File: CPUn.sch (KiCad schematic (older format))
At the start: 10 parts, among them J4 JTAG

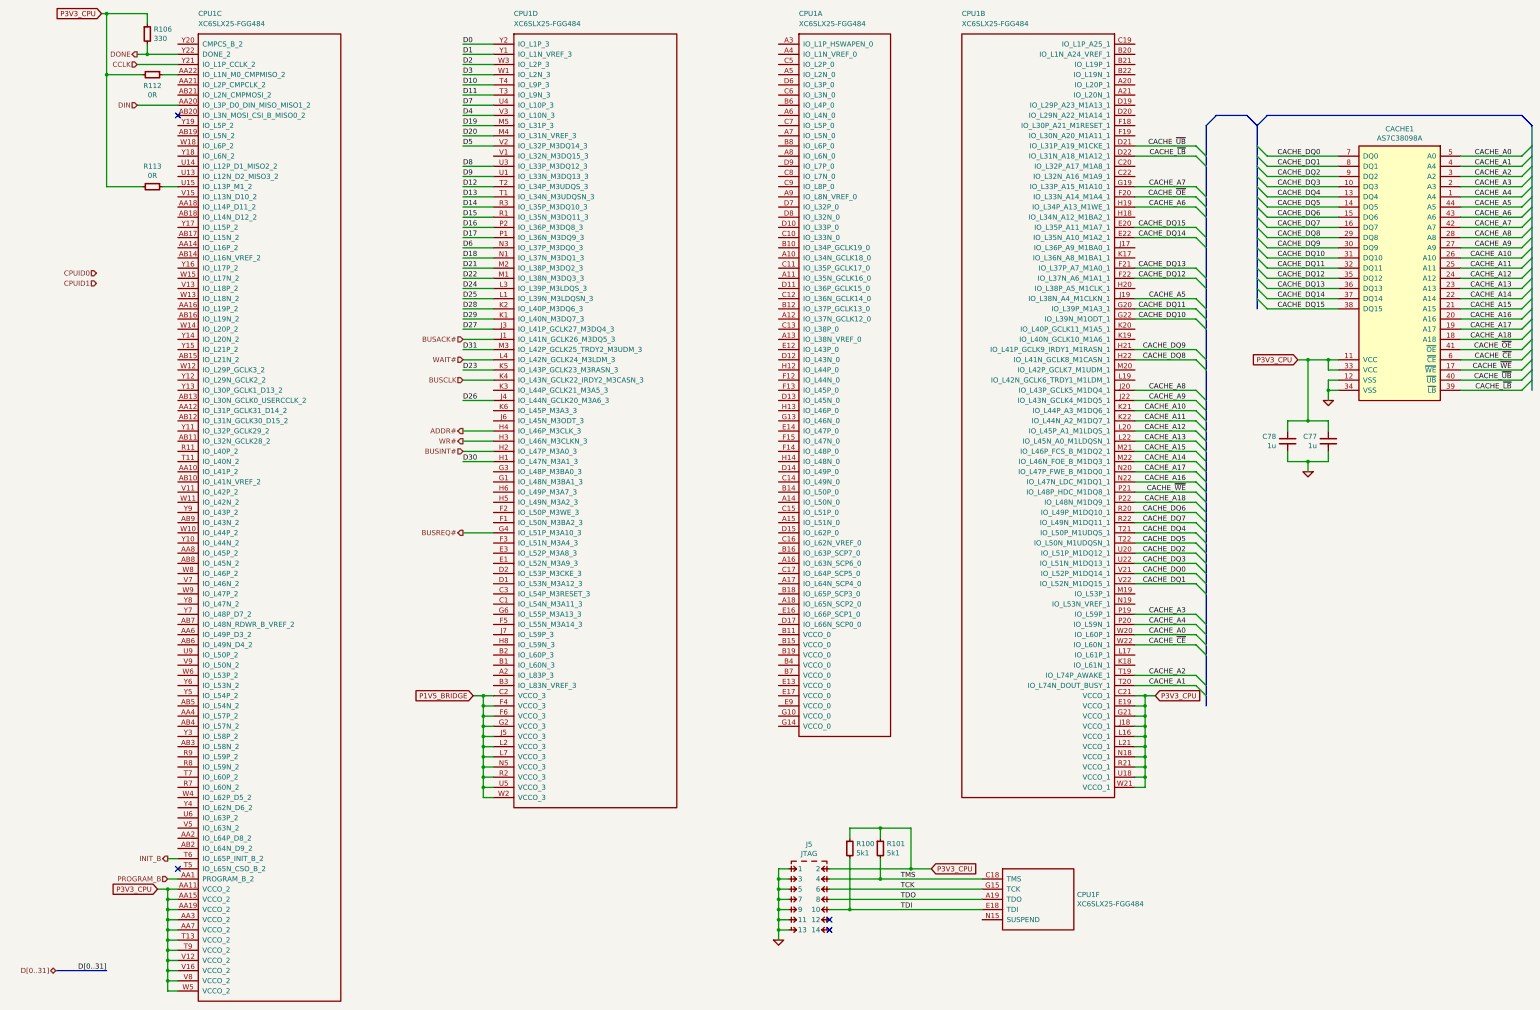
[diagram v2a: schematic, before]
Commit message: Route FPGA suspend signals
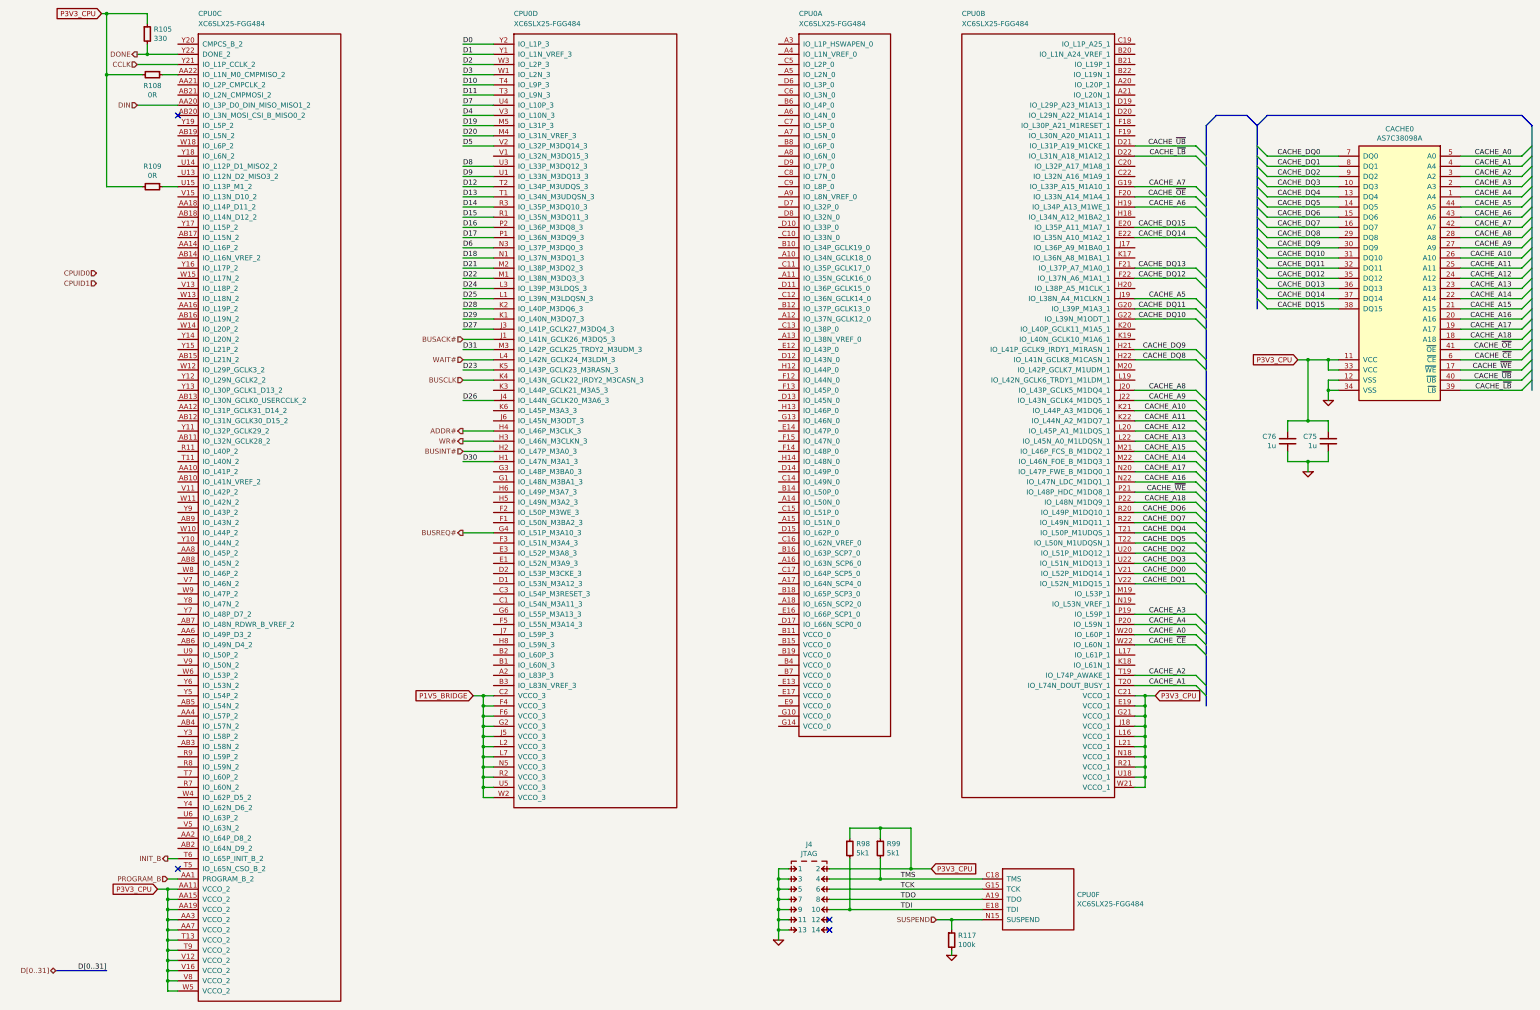
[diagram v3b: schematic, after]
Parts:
- added R117: 100k, IPC7351-Nominal:RESC1005X40, symbol R-0402
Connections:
- net GND: now also R117.2
- net SUSPEND: now reaches CPU0.N15 (SUSPEND)
- net SUSPEND: now also R117.1
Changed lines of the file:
@@
 AR Path="/5765A5BA/577B458D" Ref="CPU0"  Part="3"
 AR Path="/5765B2E6/577B458D" Ref="CPU1"  Part="3"
-F 0 "CPU1" H 2500 1300 50  0000 L CNN
+F 0 "CPU0" H 2500 1300 50  0000 L CNN
 F 1 "XC6SLX25-FGG484" H 2500 1200 50  0000 L CNN
 F 2 "manuf:XILINX-FGG484" H 2400 1150 50  0001 C CNN
@@
 AR Path="/5765A5BA/5783D342" Ref="CACHE0"  Part="1"
 AR Path="/5765B2E6/5783D342" Ref="CACHE1"  Part="1"
-F 0 "CACHE1" H 14300 2367 50  0000 C CNN
+F 0 "CACHE0" H 14300 2367 50  0000 C CNN
 F 1 "AS7C38098A" H 14300 2276 50  0000 C CNN
 F 2 "IPC7351-Nominal:SOP80P1176X120-44" H 14300 -400 50  0001 C CNN
@@
 P3V3_CPU
 $Comp
-L GND #PWR121
+L GND #PWR122
 U 1 1 5793B4AE
 P 13600 4500
-AR Path="/5765A5BA/5793B4AE" Ref="#PWR121"  Part="1"
-AR Path="/5765B2E6/5793B4AE" Ref="#PWR181"  Part="1"
-F 0 "#PWR181" H 13600 4500 30  0001 C CNN
+AR Path="/5765A5BA/5793B4AE" Ref="#PWR122"  Part="1"
+AR Path="/5765B2E6/5793B4AE" Ref="#PWR184"  Part="1"
+F 0 "#PWR122" H 13600 4500 30  0001 C CNN
 F 1 "GND" H 13600 4430 30  0001 C CNN
 F 2 "" H 13600 4500 60  0000 C CNN
@@
 AR Path="/5765A5BA/5793BAAD" Ref="C75"  Part="1"
 AR Path="/5765B2E6/5793BAAD" Ref="C77"  Part="1"
-F 0 "C77" H 13712 4946 50  0000 L CNN
+F 0 "C75" H 13712 4946 50  0000 L CNN
 F 1 "1u" H 13712 4855 50  0000 L CNN
 F 2 "IPC7351-Nominal:CAPC1005X55" H 13600 4900 50  0001 C CNN
@@
 AR Path="/5765A5BA/5793BB4A" Ref="C76"  Part="1"
 AR Path="/5765B2E6/5793BB4A" Ref="C78"  Part="1"
-F 0 "C78" H 13313 4946 50  0000 L CNN
+F 0 "C76" H 13313 4946 50  0000 L CNN
 F 1 "1u" H 13313 4855 50  0000 L CNN
 F 2 "IPC7351-Nominal:CAPC1005X55" H 13200 4900 50  0001 C CNN
@@
 $EndComp
 $Comp
-L GND #PWR120
+L GND #PWR121
 U 1 1 5793BC86
 P 13400 5200
-AR Path="/5765A5BA/5793BC86" Ref="#PWR120"  Part="1"
-AR Path="/5765B2E6/5793BC86" Ref="#PWR180"  Part="1"
-F 0 "#PWR180" H 13400 5200 30  0001 C CNN
+AR Path="/5765A5BA/5793BC86" Ref="#PWR121"  Part="1"
+AR Path="/5765B2E6/5793BC86" Ref="#PWR183"  Part="1"
+F 0 "#PWR121" H 13400 5200 30  0001 C CNN
 F 1 "GND" H 13400 5130 30  0001 C CNN
 F 2 "" H 13400 5200 60  0000 C CNN
@@
 AR Path="/5765A5BA/57942A58" Ref="CPU0"  Part="4"
 AR Path="/5765B2E6/57942A58" Ref="CPU1"  Part="4"
-F 0 "CPU1" H 5600 1300 50  0000 L CNN
+F 0 "CPU0" H 5600 1300 50  0000 L CNN
 F 1 "XC6SLX25-FGG484" H 5600 1200 50  0000 L CNN
 F 2 "manuf:XILINX-FGG484" H 5500 1150 50  0001 C CNN
@@
 AR Path="/5765A5BA/5795C53B" Ref="CPU0"  Part="1"
 AR Path="/5765B2E6/5795C53B" Ref="CPU1"  Part="1"
-F 0 "CPU1" H 8400 1300 50  0000 L CNN
+F 0 "CPU0" H 8400 1300 50  0000 L CNN
 F 1 "XC6SLX25-FGG484" H 8400 1200 50  0000 L CNN
 F 2 "manuf:XILINX-FGG484" H 8300 1150 50  0001 C CNN
@@
 AR Path="/5765A5BA/5795C751" Ref="CPU0"  Part="2"
 AR Path="/5765B2E6/5795C751" Ref="CPU1"  Part="2"
-F 0 "CPU1" H 13400 1300 50  0000 R CNN
+F 0 "CPU0" H 13400 1300 50  0000 R CNN
 F 1 "XC6SLX25-FGG484" H 13400 1200 50  0000 R CNN
 F 2 "manuf:XILINX-FGG484" H 11800 1150 50  0001 C CNN
@@
 AR Path="/5765A5BA/57A58F79" Ref="R105"  Part="1"
 AR Path="/5765B2E6/57A58F79" Ref="R106"  Part="1"
-F 0 "R106" H 2063 946 50  0000 L CNN
+F 0 "R105" H 2063 946 50  0000 L CNN
 F 1 "330" H 2063 855 50  0000 L CNN
 F 2 "IPC7351-Nominal:RESC1005X40" H 2000 900 50  0001 C CNN
@@
 AR Path="/5765A5BA/57A5D20B" Ref="R108"  Part="1"
 AR Path="/5765B2E6/57A5D20B" Ref="R112"  Part="1"
-F 0 "R112" V 2158 1300 50  0000 C CNN
+F 0 "R108" V 2158 1300 50  0000 C CNN
 F 1 "0R" V 2249 1300 50  0000 C CNN
 F 2 "IPC7351-Nominal:RESC1005X40" H 2050 1300 50  0001 C CNN
@@
 AR Path="/5765A5BA/57A5D251" Ref="R109"  Part="1"
 AR Path="/5765B2E6/57A5D251" Ref="R113"  Part="1"
-F 0 "R113" V 1850 2400 50  0000 C CNN
+F 0 "R109" V 1850 2400 50  0000 C CNN
 F 1 "0R" V 1941 2400 50  0000 C CNN
 F 2 "IPC7351-Nominal:RESC1005X40" H 2050 2400 50  0001 C CNN
@@
 AR Path="/5765A5BA/57A7F2F7" Ref="J4"  Part="1"
 AR Path="/5765B2E6/57A7F2F7" Ref="J5"  Part="1"
-F 0 "J5" H 8500 9340 50  0000 C CNN
+F 0 "J4" H 8500 9340 50  0000 C CNN
 F 1 "JTAG" H 8500 9249 50  0000 C CNN
 F 2 "conn-fci:98424-G52-14ALF" H 8475 9100 50  0001 C CNN
@@
 P 8200 9800
 AR Path="/5763AB3B/57A7F302" Ref="#PWR?"  Part="1"
-AR Path="/5765B2E6/57A7F302" Ref="#PWR179"  Part="1"
+AR Path="/5765B2E6/57A7F302" Ref="#PWR181"  Part="1"
 AR Path="/5765A5BA/57A7F302" Ref="#PWR119"  Part="1"
-F 0 "#PWR179" H 8200 9800 30  0001 C CNN
+F 0 "#PWR119" H 8200 9800 30  0001 C CNN
 F 1 "GND" H 8200 9730 30  0001 C CNN
 F 2 "" H 8200 9800 60  0000 C CNN
@@
 AR Path="/5765A5BA/57A7F317" Ref="R98"  Part="1"
 AR Path="/5765B2E6/57A7F317" Ref="R100"  Part="1"
-F 0 "R100" H 8963 8946 50  0000 L CNN
+F 0 "R98" H 8963 8946 50  0000 L CNN
 F 1 "5k1" H 8963 8855 50  0000 L CNN
 F 2 "IPC7351-Nominal:RESC1005X40" H 8900 8900 50  0001 C CNN
@@
 AR Path="/5765A5BA/57A7F321" Ref="R99"  Part="1"
 AR Path="/5765B2E6/57A7F321" Ref="R101"  Part="1"
-F 0 "R101" H 9263 8946 50  0000 L CNN
+F 0 "R99" H 9263 8946 50  0000 L CNN
 F 1 "5k1" H 9263 8855 50  0000 L CNN
 F 2 "IPC7351-Nominal:RESC1005X40" H 9200 8900 50  0001 C CNN
@@
 AR Path="/5765A5BA/57A7F34A" Ref="CPU0"  Part="6"
 AR Path="/5765B2E6/57A7F34A" Ref="CPU1"  Part="6"
-F 0 "CPU1" H 11131 9046 50  0000 L CNN
+F 0 "CPU0" H 11131 9046 50  0000 L CNN
 F 1 "XC6SLX25-FGG484" H 11131 8955 50  0000 L CNN
 F 2 "manuf:XILINX-FGG484" H 10300 9350 50  0001 C CNN
@@
 Wire Bus Line
 	15600 1800 15600 4400
+$Comp
+L R-0402 R?
+U 1 1 57A6CB4C
+P 9900 9800
+AR Path="/5763AB3B/57A6CB4C" Ref="R?"  Part="1"
+AR Path="/5765A5BA/57A6CB4C" Ref="R117"  Part="1"
+AR Path="/5765B2E6/57A6CB4C" Ref="R119"  Part="1"
+F 0 "R117" H 9963 9846 50  0000 L CNN
+F 1 "100k" H 9963 9755 50  0000 L CNN
+F 2 "IPC7351-Nominal:RESC1005X40" H 9900 9800 50  0001 C CNN
+F 3 "" H 9900 9850 60  0000 C CNN
+F 4 "RES SMD 100k 1% [0402]" H 10650 10350 60  0001 C CNN "BOM"
+	1    9900 9800
+	1    0    0    -1
+$EndComp
+Wire Wire Line
+	9750 9600 10200 9600
+Wire Wire Line
+	9900 9600 9900 9700
+$Comp
+L GND #PWR120
+U 1 1 57A6CCC5
+P 9900 9950
+AR Path="/5765A5BA/57A6CCC5" Ref="#PWR120"  Part="1"
+AR Path="/5765B2E6/57A6CCC5" Ref="#PWR182"  Part="1"
+F 0 "#PWR120" H 9900 9950 30  0001 C CNN
+F 1 "GND" H 9900 9880 30  0001 C CNN
+F 2 "" H 9900 9950 60  0000 C CNN
+F 3 "" H 9900 9950 60  0000 C CNN
+	1    9900 9950
+	1    0    0    -1
+$EndComp
+Wire Wire Line
+	9900 9950 9900 9900
+Text HLabel 9750 9600 0    50   Input ~ 0
+SUSPEND
+Connection ~ 9900 9600
 $EndSCHEMATC

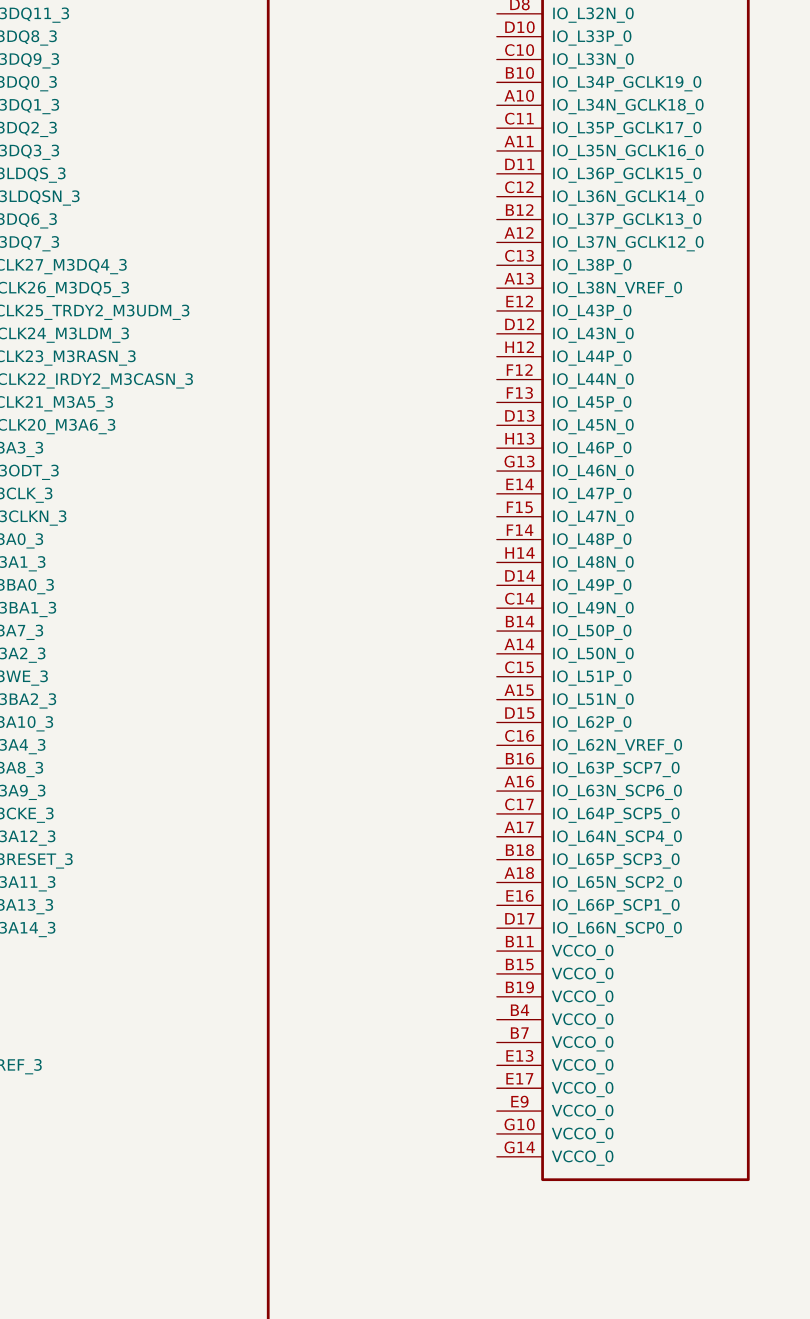
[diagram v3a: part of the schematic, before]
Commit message: Add inter-CPU handshake lines
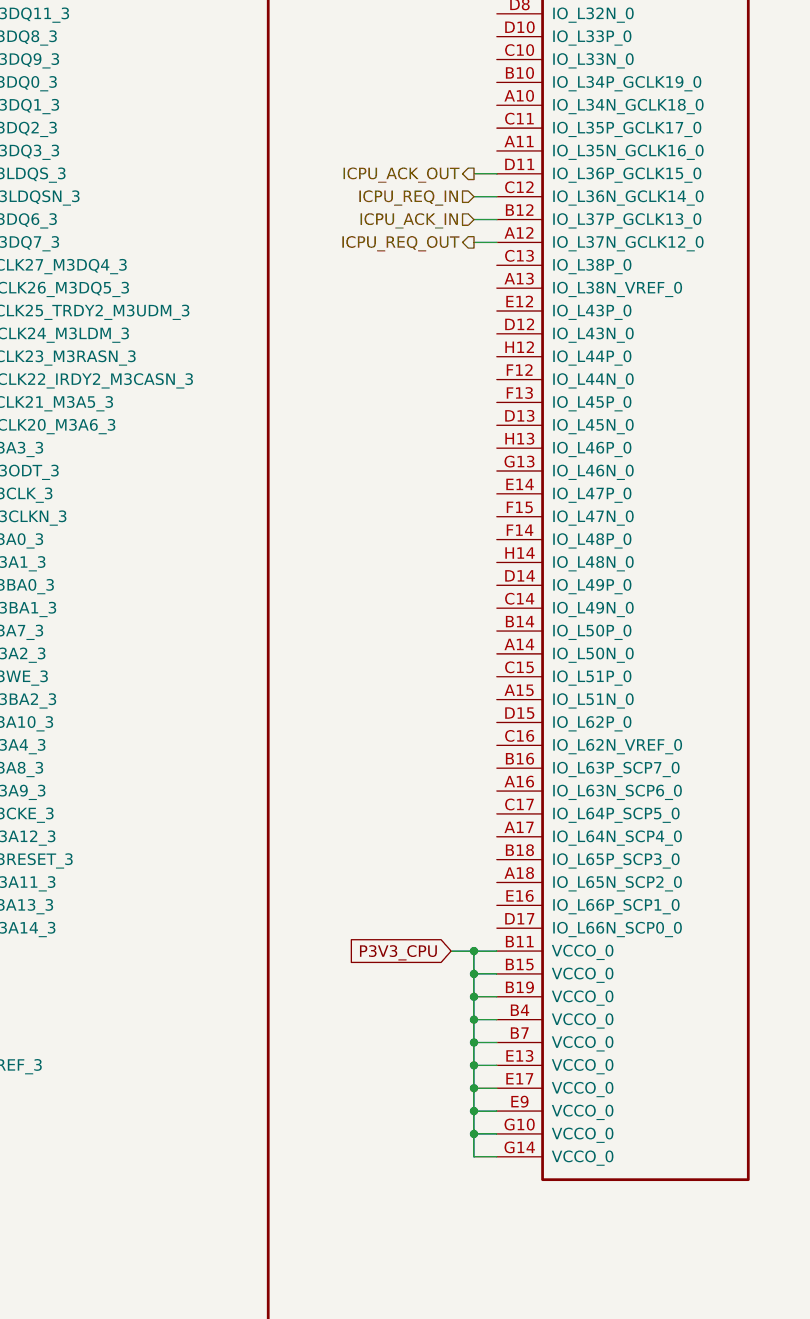
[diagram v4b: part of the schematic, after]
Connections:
- net P3V3_CPU: now also CPU0.B11 (VCCO_0), CPU0.B15 (VCCO_0), CPU0.B19 (VCCO_0), CPU0.B4 (VCCO_0), CPU0.B7 (VCCO_0), CPU0.E13 (VCCO_0), CPU0.E17 (VCCO_0), CPU0.E9 (VCCO_0), CPU0.G10 (VCCO_0), CPU0.G14 (VCCO_0)
- net ICPU_REQ_OUT: now reaches CPU0.A12 (IO_L37N_GCLK12_0)
- net ICPU_ACK_IN: now reaches CPU0.B12 (IO_L37P_GCLK13_0)
- net ICPU_REQ_IN: now reaches CPU0.C12 (IO_L36N_GCLK14_0)
- net ICPU_ACK_OUT: now reaches CPU0.D11 (IO_L36P_GCLK15_0)
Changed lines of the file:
@@
 SUSPEND
 Connection ~ 9900 9600
+Text GLabel 8000 6800 0    50   Input ~ 0
+P3V3_CPU
+Wire Wire Line
+	8000 6800 8200 6800
+Wire Wire Line
+	8100 6900 8200 6900
+Wire Wire Line
+	8100 7000 8200 7000
+Wire Wire Line
+	8100 7100 8200 7100
+Wire Wire Line
+	8100 7200 8200 7200
+Wire Wire Line
+	8100 7300 8200 7300
+Wire Wire Line
+	8100 7400 8200 7400
+Wire Wire Line
+	8100 7500 8200 7500
+Wire Wire Line
+	8100 7600 8200 7600
+Wire Wire Line
+	8100 7700 8200 7700
+Connection ~ 8100 6800
+Connection ~ 8100 6900
+Connection ~ 8100 7000
+Connection ~ 8100 7100
+Connection ~ 8100 7200
+Connection ~ 8100 7300
+Connection ~ 8100 7400
+Connection ~ 8100 7500
+Connection ~ 8100 7600
+Wire Wire Line
+	8100 6800 8100 7700
+Text HLabel 8100 3700 0    50   Output ~ 0
+ICPU_REQ_OUT
+Wire Wire Line
+	8200 3700 8100 3700
+Text HLabel 8100 3600 0    50   Input ~ 0
+ICPU_ACK_IN
+Wire Wire Line
+	8100 3600 8200 3600
+Text HLabel 8100 3500 0    50   Input ~ 0
+ICPU_REQ_IN
+Wire Wire Line
+	8100 3500 8200 3500
+Text HLabel 8100 3400 0    50   Output ~ 0
+ICPU_ACK_OUT
+Wire Wire Line
+	8100 3400 8200 3400
 $EndSCHEMATC
